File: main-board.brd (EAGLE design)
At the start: 49.2 x 17.8 mm, 54 parts, among them IC1 MEGA328-PB, IC2 MCP73831, IC3 LE33, Q1 3,6864 MHz, Q4 TSM2302CX, T1 IRF7306

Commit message: Create nice place views.
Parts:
- LED2: value YELLOW -> YEL
- LED3: value GREEN -> GR

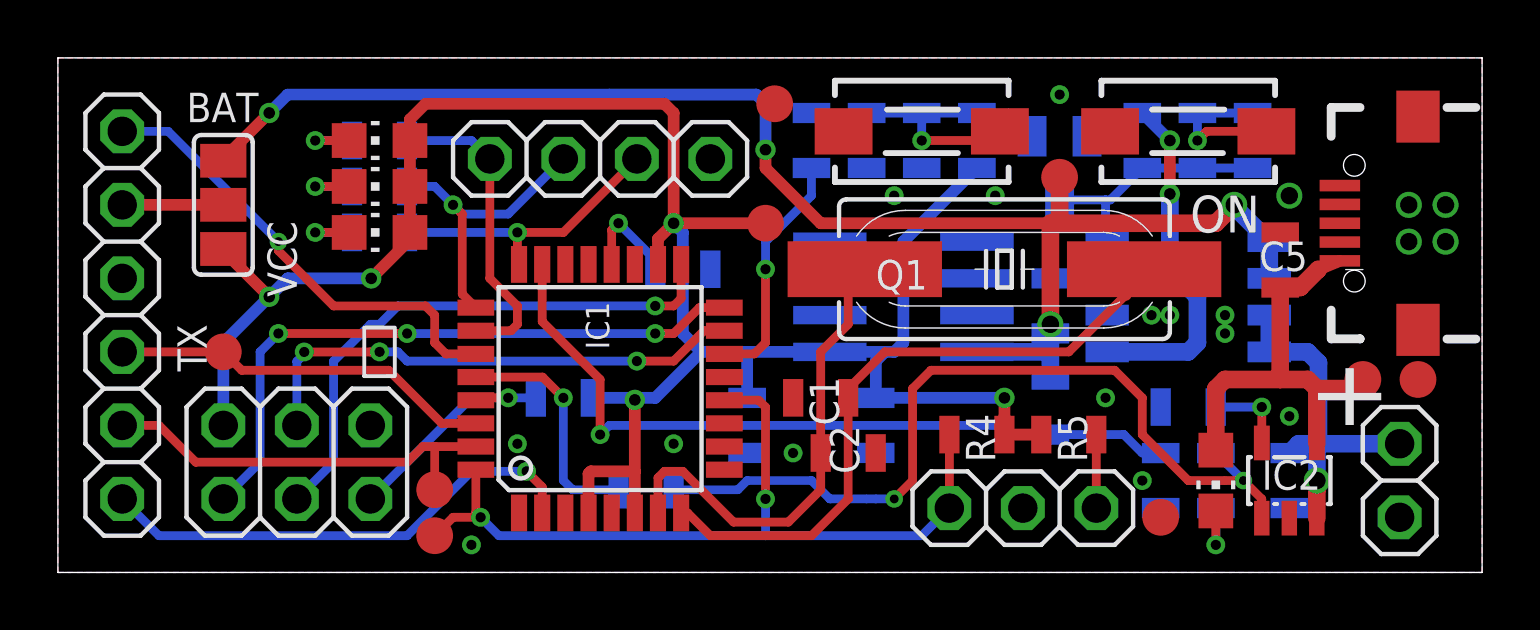
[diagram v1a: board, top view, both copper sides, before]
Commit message: Fix shutdown circuit.
Shutting down from CPU should work now.
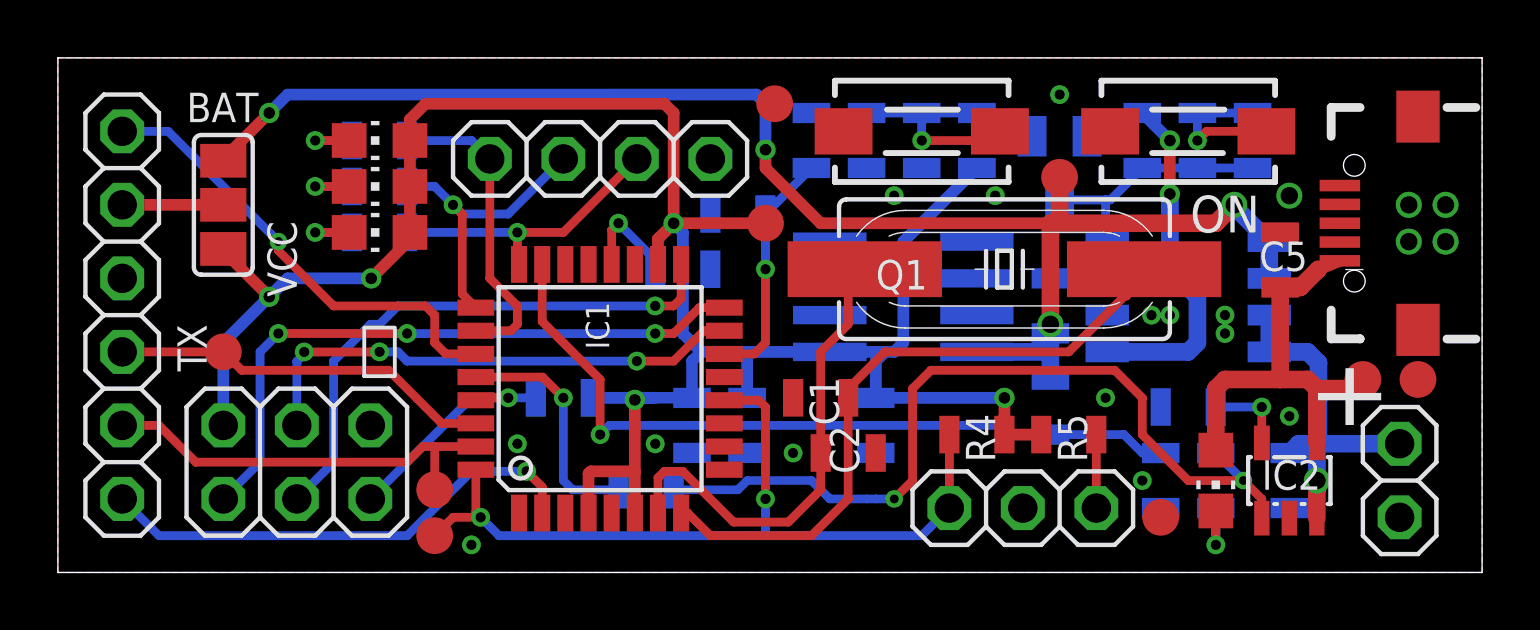
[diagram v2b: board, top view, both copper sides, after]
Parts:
- added C10: 100n, rcl:C0805
- added R16: 2k, rcl:R0805
- C9: value 100n -> 10n
- R13: value 10K -> 200k
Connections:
- net !SHUTDOWN: now also C10.1
- net GND: now also C10.2, R16.2
- net VCC: now also R16.1
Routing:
- net VCC: track 76.3 -> 77.4 mm
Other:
- board text added: "WSM v1.3"
- board text removed: "WSM v1.2"
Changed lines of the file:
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@@
 <text x="8.255" y="9.525" size="1.016" layer="25" rot="R90">VCC</text>
 <text x="40.3225" y="11.7475" size="1.27" layer="25" rot="R180" align="top-center">ON</text>
-<text x="48.26" y="16.8275" size="1.778" layer="26" rot="MR270">WSM v1.2</text>
+<text x="48.26" y="16.8275" size="1.778" layer="26" rot="MR270">WSM v1.3</text>
 </plain>
 <attributes>
@@
 <attribute name="VALUE" x="43.4975" y="16.51" size="1.27" layer="28" rot="MR270"/>
 </element>
-<element name="C9" library="rcl" package="C0805" value="100n" x="27.94" y="14.9225" smashed="yes" rot="MR270">
+<element name="C9" library="rcl" package="C0805" value="10n" x="27.94" y="14.9225" smashed="yes" rot="MR270">
 <attribute name="NAME" x="26.9875" y="13.335" size="1.016" layer="26" rot="MR180"/>
 <attribute name="VALUE" x="26.035" y="17.4625" size="1.27" layer="28" rot="MR180"/>
@@
 <attribute name="VALUE" x="28.8925" y="13.6525" size="1.27" layer="28" rot="MR180"/>
 </element>
-<element name="R13" library="rcl" package="R0805" value="10K" x="31.75" y="14.9225" smashed="yes" rot="MR90">
+<element name="R13" library="rcl" package="R0805" value="200k" x="31.75" y="14.9225" smashed="yes" rot="MR90">
 <attribute name="NAME" x="33.02" y="12.3825" size="1.016" layer="26" rot="MR0"/>
 <attribute name="VALUE" x="33.3375" y="16.1925" size="1.27" layer="28" rot="MR0"/>
@@
 <attribute name="VALUE" x="14.9225" y="1.905" size="1.27" layer="28" rot="MR180"/>
 </element>
+<element name="C10" library="rcl" package="C0805" value="100n" x="23.495" y="12.3825" rot="MR0"/>
+<element name="R16" library="rcl" package="R0805" value="2k" x="21.9075" y="5.08" rot="MR270"/>
 </elements>
 <signals>
@@
 <via x="25.4" y="4.1275" extent="1-16" drill="0.35"/>
 <via x="15.875" y="4.445" extent="1-16" drill="0.35"/>
-<via x="21.2725" y="4.445" extent="1-16" drill="0.35"/>
+<via x="20.6375" y="4.445" extent="1-16" drill="0.35"/>
 <via x="46.6725" y="12.7" extent="1-16" drill="0.6"/>
 <via x="46.6725" y="11.43" extent="1-16" drill="0.6"/>
@@
 <via x="40.3225" y="8.255" extent="1-16" drill="0.35"/>
 <via x="32.385" y="13.0175" extent="1-16" drill="0.35"/>
+<contactref element="C10" pad="2"/>
+<contactref element="R16" pad="2"/>
 </signal>
 <signal name="VCC" class="2">
@@
 <wire x1="18.4125" y1="6.0325" x2="19.8625" y2="6.0325" width="0.4064" layer="16"/>
 <wire x1="19.8625" y1="6.0325" x2="19.9325" y2="5.9625" width="0.4064" layer="16"/>
-<wire x1="22.225" y1="7.62" x2="20.6375" y2="6.0325" width="0.4064" layer="16"/>
-<wire x1="20.6375" y1="6.0325" x2="19.8625" y2="6.0325" width="0.4064" layer="16"/>
+<wire x1="20.6375" y1="6.0325" x2="20.32" y2="6.0325" width="0.4064" layer="16"/>
+<wire x1="20.32" y1="6.0325" x2="19.8625" y2="6.0325" width="0.4064" layer="16"/>
 <wire x1="32.7025" y1="6.0325" x2="28.26" y2="6.0325" width="0.4064" layer="16"/>
 <wire x1="28.26" y1="6.0325" x2="28.2575" y2="6.03" width="0.4064" layer="16"/>
@@
 <wire x1="7.3025" y1="9.525" x2="5.969" y2="10.8585" width="0.4" layer="1"/>
 <wire x1="5.969" y1="10.8585" x2="5.969" y2="11.176" width="0.4" layer="1"/>
+<contactref element="R16" pad="1"/>
+<wire x1="20.32" y1="6.0325" x2="21.905" y2="6.0325" width="0.4" layer="16"/>
+<wire x1="21.905" y1="6.0325" x2="21.9075" y2="6.03" width="0.4" layer="16"/>
+<wire x1="21.9075" y1="6.03" x2="21.9075" y2="7.3025" width="0.4" layer="16"/>
+<wire x1="21.9075" y1="7.3025" x2="22.225" y2="7.62" width="0.4" layer="16"/>
 </signal>
 <signal name="LED-RED-R">
@@
 <contactref element="R15" pad="1"/>
 <contactref element="IC1" pad="14"/>
-<wire x1="26.035" y1="13.9725" x2="26.035" y2="13.0175" width="0.3048" layer="16"/>
 <wire x1="24.06" y1="7.55" x2="23.0251" y2="7.55" width="0.3048" layer="1"/>
 <wire x1="24.06" y1="7.55" x2="24.4475" y2="7.9375" width="0.3048" layer="1"/>
@@
 <via x="24.4475" y="10.4775" extent="1-16" drill="0.35"/>
 <wire x1="24.4475" y1="10.4775" x2="24.4475" y2="11.43" width="0.3048" layer="16"/>
-<wire x1="24.4475" y1="11.43" x2="26.035" y2="13.0175" width="0.3048" layer="16"/>
+<contactref element="C10" pad="1"/>
+<wire x1="24.4475" y1="11.43" x2="24.445" y2="11.4325" width="0.3" layer="16"/>
+<wire x1="24.445" y1="11.4325" x2="24.445" y2="12.3825" width="0.3" layer="16"/>
+<wire x1="24.445" y1="12.3825" x2="26.035" y2="13.9725" width="0.3" layer="16"/>
 </signal>
 <signal name="BAT-RAW-VCC" class="1">

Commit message: Change voltage divisor (use LDO as reference).
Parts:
- R16: value 2k -> 2K
- R7: value 680K -> 4K
- R8: value 200K -> 10K
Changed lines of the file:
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@@
 <attribute name="VALUE" x="19.05" y="6.985" size="1.27" layer="28" rot="MR0"/>
 </element>
-<element name="R7" library="rcl" package="R0805" value="680K" x="34.29" y="5.715" smashed="yes" rot="MR90">
+<element name="R7" library="rcl" package="R0805" value="4K" x="34.29" y="5.715" smashed="yes" rot="MR90">
 <attribute name="NAME" x="35.2425" y="5.08" size="1.016" layer="26" rot="MR90"/>
 <attribute name="VALUE" x="33.3375" y="7.62" size="1.27" layer="28" rot="MR270"/>
 </element>
-<element name="R8" library="rcl" package="R0805" value="200K" x="38.1" y="3.175" smashed="yes" rot="MR90">
+<element name="R8" library="rcl" package="R0805" value="10K" x="38.1" y="3.175" smashed="yes" rot="MR90">
 <attribute name="NAME" x="37.1475" y="1.5875" size="1.016" layer="26" rot="MR180"/>
 <attribute name="VALUE" x="38.735" y="1.5875" size="1.27" layer="28" rot="MR270"/>
@@
 </element>
 <element name="C10" library="rcl" package="C0805" value="100n" x="23.495" y="12.3825" rot="MR0"/>
-<element name="R16" library="rcl" package="R0805" value="2k" x="21.9075" y="5.08" rot="MR270"/>
+<element name="R16" library="rcl" package="R0805" value="2K" x="21.9075" y="5.08" rot="MR270"/>
 </elements>
 <signals>

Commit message: 4K -> 3K9.
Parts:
- R4: value 10K -> 3K9
- R7: value 4K -> 3K9
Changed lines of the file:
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@@
 <attribute name="NAME" x="9.525" y="11.1125" size="1.27" layer="26" rot="MR0"/>
 </element>
-<element name="R4" library="rcl" package="R0805" value="10K" x="31.75" y="4.7625" smashed="yes">
+<element name="R4" library="rcl" package="R0805" value="3K9" x="31.75" y="4.7625" smashed="yes">
 <attribute name="NAME" x="32.385" y="3.81" size="1.016" layer="25" rot="R90"/>
 <attribute name="VALUE" x="30.1625" y="3.81" size="1.27" layer="27" rot="R90"/>
@@
 <attribute name="VALUE" x="19.05" y="6.985" size="1.27" layer="28" rot="MR0"/>
 </element>
-<element name="R7" library="rcl" package="R0805" value="4K" x="34.29" y="5.715" smashed="yes" rot="MR90">
+<element name="R7" library="rcl" package="R0805" value="3K9" x="34.29" y="5.715" smashed="yes" rot="MR90">
 <attribute name="NAME" x="35.2425" y="5.08" size="1.016" layer="26" rot="MR90"/>
 <attribute name="VALUE" x="33.3375" y="7.62" size="1.27" layer="28" rot="MR270"/>
